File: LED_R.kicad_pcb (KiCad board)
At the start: 2 copper layers, 12 x 23.2 mm, 18 parts, among them J1 Conn_01x08, J2 Conn_01x08

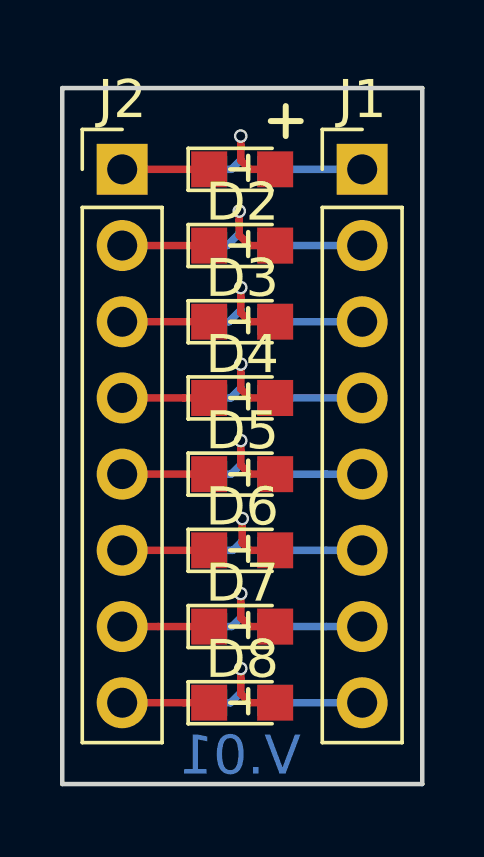
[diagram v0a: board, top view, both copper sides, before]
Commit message: changed the text size and position
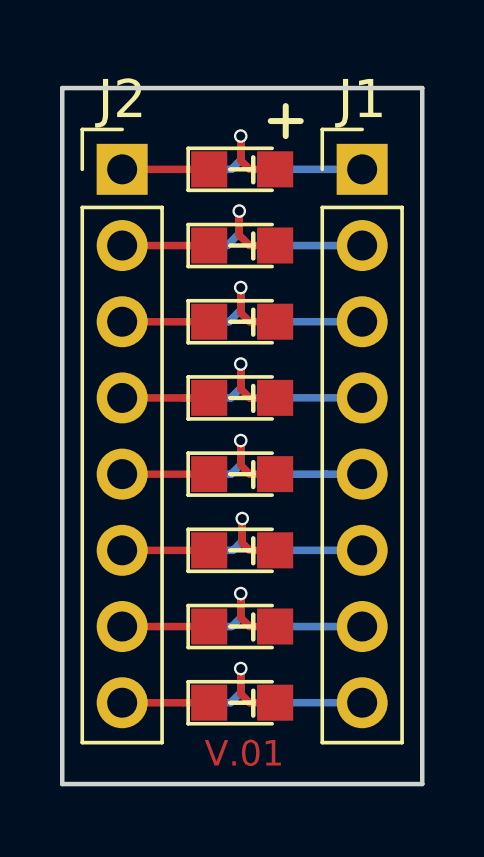
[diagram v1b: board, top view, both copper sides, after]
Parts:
- D1, D2, D3, D4, D5, D6, D7, D8: footprint LED0805:LED_0805 -> MetalPad:LED_0805
